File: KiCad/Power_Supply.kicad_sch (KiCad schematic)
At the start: 4 parts, among them J1 USB_B, J2 Jack-DC

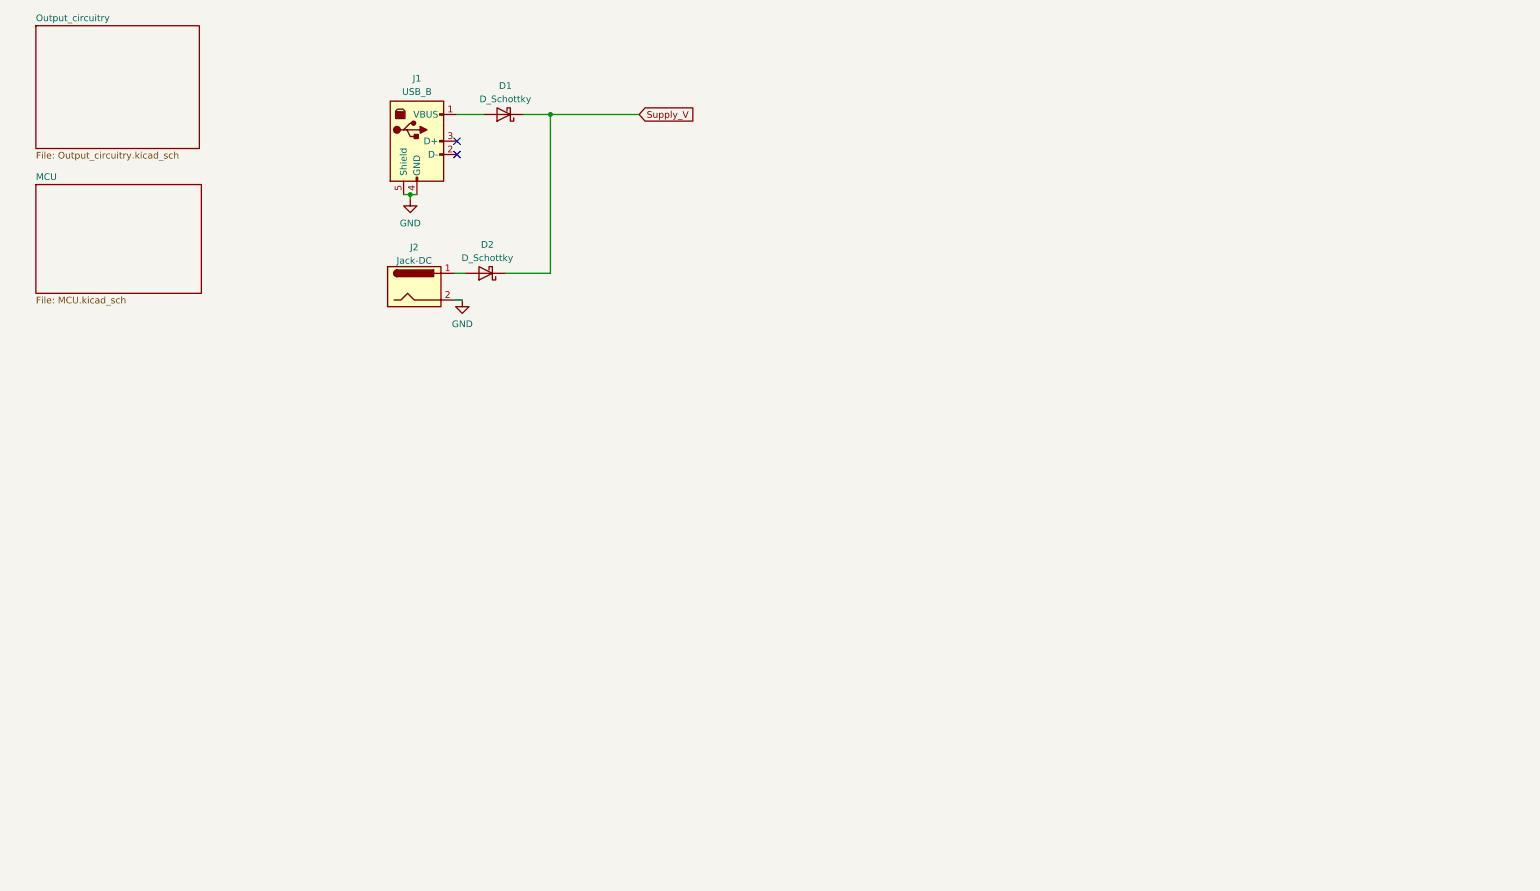
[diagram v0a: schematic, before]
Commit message: Schematic redesign needs two footprints before complete.
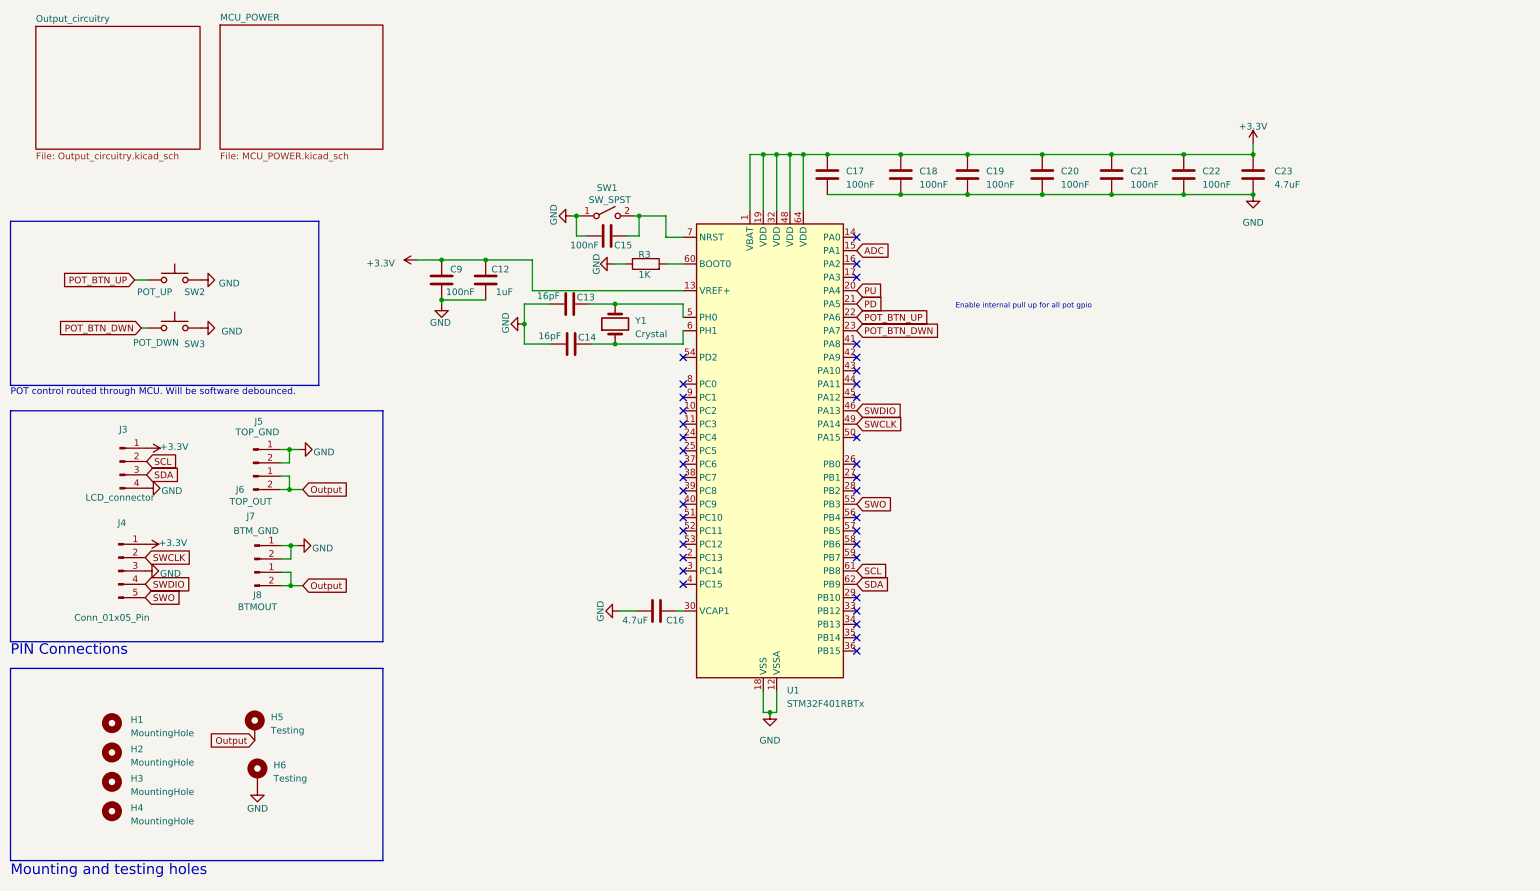
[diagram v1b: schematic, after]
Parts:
- removed D1, D2: D_Schottky, symbol Device:D_Schottky
- removed J1: USB_B, symbol Connector:USB_B
- removed J2: Jack-DC, symbol Connector:Jack-DC
- added C12: 1uF, Capacitor_SMD:C_0603_1608Metric_Pad1.08x0.95mm_HandSolder, symbol Device:C
- added C13, C14: 16pF, Capacitor_SMD:C_0603_1608Metric_Pad1.08x0.95mm_HandSolder, symbol Device:C
- added C15, C17, C18, C19, C20, C21, C22, C9: 100nF, Capacitor_SMD:C_0603_1608Metric_Pad1.08x0.95mm_HandSolder, symbol Device:C
- added C16, C23: 4.7uF, Capacitor_SMD:C_0603_1608Metric_Pad1.08x0.95mm_HandSolder, symbol Device:C
- added H1, H2, H3, H4: MountingHole, MountingHole:MountingHole_3.2mm_M3, symbol Mechanical:MountingHole
- added H5, H6: Testing, MountingHole:MountingHole_2.2mm_M2_DIN965_Pad_TopOnly, symbol Mechanical:MountingHole_Pad
- added J3: LCD_connector, Connector_PinHeader_2.54mm:PinHeader_1x04_P2.54mm_Vertical, symbol Connector:Conn_01x04_Pin
- added J4: Conn_01x05_Pin, Connector_PinHeader_2.54mm:PinHeader_1x05_P2.54mm_Vertical, symbol Connector:Conn_01x05_Pin
- added J5: TOP_GND, Connector_PinHeader_2.54mm:PinHeader_1x02_P2.54mm_Vertical, symbol Connector:Conn_01x02_Pin
- added J6: TOP_OUT, Connector_PinHeader_2.54mm:PinHeader_1x02_P2.54mm_Vertical, symbol Connector:Conn_01x02_Pin
- added J7: BTM_GND, Connector_PinHeader_2.54mm:PinHeader_1x02_P2.54mm_Vertical, symbol Connector:Conn_01x02_Pin
- added J8: BTMOUT, Connector_PinHeader_2.54mm:PinHeader_1x02_P2.54mm_Vertical, symbol Connector:Conn_01x02_Pin
- added R3: 1K, Resistor_SMD:R_0402_1005Metric_Pad0.72x0.64mm_HandSolder, symbol Device:R
- added SW1: SW_SPST, symbol Switch:SW_SPST
- added SW2: POT_UP, Button_Switch_THT:SW_PUSH_6mm_H4.3mm, symbol Switch:SW_Push
- added SW3: POT_DWN, Button_Switch_THT:SW_PUSH_6mm_H4.3mm, symbol Switch:SW_Push
- added U1: STM32F401RBTx, Package_QFP:LQFP-64_10x10mm_P0.5mm, symbol MCU_ST_STM32F4:STM32F401RBTx
- added Y1: Crystal, Crystal:Crystal_SMD_ECS_CSM3X-2Pin_7.6x4.1mm, symbol Device:Crystal
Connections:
- net GND: now also C12.1, C13.1, C14.1, C15.1, C16.1, C17.2, C18.2, C19.2, C20.2, C21.2, C22.2, C23.2, C9.1, H6.1, J3.4 (Pin_4), J4.3 (Pin_3), J5.1 (Pin_1), J5.2 (Pin_2), J7.1 (Pin_1), J7.2 (Pin_2), R3.1, SW1.1 (A), SW2.2, SW3.2, U1.12 (VSSA), U1.18 (VSS), U1.31 (VSS), U1.47 (VSS), U1.63 (VSS)
- new net: C16.2, U1.30 (VCAP1)
- new net: C13.2, U1.5 (PH0), Y1.2
- new net: C14.2, U1.6 (PH1), Y1.1
- new net: R3.2, U1.60 (BOOT0)
- new net: C15.2, SW1.2 (B), U1.7 (NRST)
- new net +3.3V: C12.2, C17.1, C18.1, C19.1, C20.1, C21.1, C22.1, C23.1, C9.2, J3.1 (Pin_1), J4.1 (Pin_1), U1.1 (VBAT), U1.13 (VREF+), U1.19 (VDD), U1.32 (VDD), U1.48 (VDD), U1.64 (VDD)
- new net ADC: U1.15 (PA1)
- new net Output: H5.1, J6.1 (Pin_1), J6.2 (Pin_2), J8.1 (Pin_1), J8.2 (Pin_2)
- new net PD: U1.21 (PA5)
- new net POT_BTN_DWN: SW3.1, U1.23 (PA7)
- new net POT_BTN_UP: SW2.1, U1.22 (PA6)
- new net PU: U1.20 (PA4)
- new net SCL: J3.2 (Pin_2), U1.61 (PB8)
- new net SDA: J3.3 (Pin_3), U1.62 (PB9)
- new net SWCLK: J4.2 (Pin_2), U1.49 (PA14)
- new net SWDIO: J4.4 (Pin_4), U1.46 (PA13)
- new net SWO: J4.5 (Pin_5), U1.55 (PB3)
- no-connect marks 2 -> 38
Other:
- removed sheet MCU
- added sheet MCU_POWER (MCU_POWER.kicad_sch)
- note added: "Enable internal pull up for all pot gpio"
- note added: "Mounting and testing holes"
- note added: "PIN Connections"
- note added: "POT control routed through MCU. Will be software debounced."
- company: (none) -> Eric Mullally
- title: (none) -> Power Supply

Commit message: Board layout preleminary complete.
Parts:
- removed J5: TOP_GND, Connector_PinHeader_2.54mm:PinHeader_1x02_P2.54mm_Vertical, symbol Connector:Conn_01x02_Pin
- removed J6: TOP_OUT, Connector_PinHeader_2.54mm:PinHeader_1x02_P2.54mm_Vertical, symbol Connector:Conn_01x02_Pin
- removed J7: BTM_GND, Connector_PinHeader_2.54mm:PinHeader_1x02_P2.54mm_Vertical, symbol Connector:Conn_01x02_Pin
- removed J8: BTMOUT, Connector_PinHeader_2.54mm:PinHeader_1x02_P2.54mm_Vertical, symbol Connector:Conn_01x02_Pin
- removed SW1: SW_SPST, symbol Switch:SW_SPST
- added J10: BTM_OUT, Connector_PinHeader_2.54mm:PinHeader_2x02_P2.54mm_Vertical, symbol Connector_Generic:Conn_02x02_Top_Bottom
- added J5: TOP_OUT, Connector_PinHeader_2.54mm:PinHeader_2x02_P2.54mm_Vertical, symbol Connector_Generic:Conn_02x02_Top_Bottom
- added R5: 100, Resistor_SMD:R_0402_1005Metric_Pad0.72x0.64mm_HandSolder, symbol Device:R
- added R6: 300, Resistor_SMD:R_0402_1005Metric_Pad0.72x0.64mm_HandSolder, symbol Device:R
- added SW1: NRST, Button_Switch_THT:SW_PUSH_6mm_H4.3mm, symbol Switch:SW_Push
- J4: value Conn_01x05_Pin -> SWD
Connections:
- net ADC: now also R5.2, R6.2; no longer U1.15 (PA1)
- net GND: now also J10.3 (Pin_3), J10.4 (Pin_4), J5.3 (Pin_3), J5.4 (Pin_4), R6.1, SW1.1
- net Output: now also J10.1 (Pin_1), J10.2 (Pin_2), J5.1 (Pin_1), J5.2 (Pin_2)
- net VCAP: now reaches C16.2, U1.30 (VCAP1)
- net BOOT: now reaches R3.2, U1.60 (BOOT0)
- net NRST: now reaches C15.2, U1.7 (NRST)
- net NRST: now also SW1.2
- new net: R5.1, U1.15 (PA1)
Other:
- moved on the sheet: C16, R3

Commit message: Boot-0 and button layout updated.
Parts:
- added R7: 1K, Resistor_SMD:R_0402_1005Metric_Pad0.72x0.64mm_HandSolder, symbol Device:R
- R5: value 100 -> 300
- R6: value 300 -> 1K2
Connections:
- net +3.3V: now also R7.1
- net BOOT: now also R7.2
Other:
- note added: "Notes"
- note removed: "Enable internal pull up for all pot gpio"
- moved on the sheet: C15, SW1

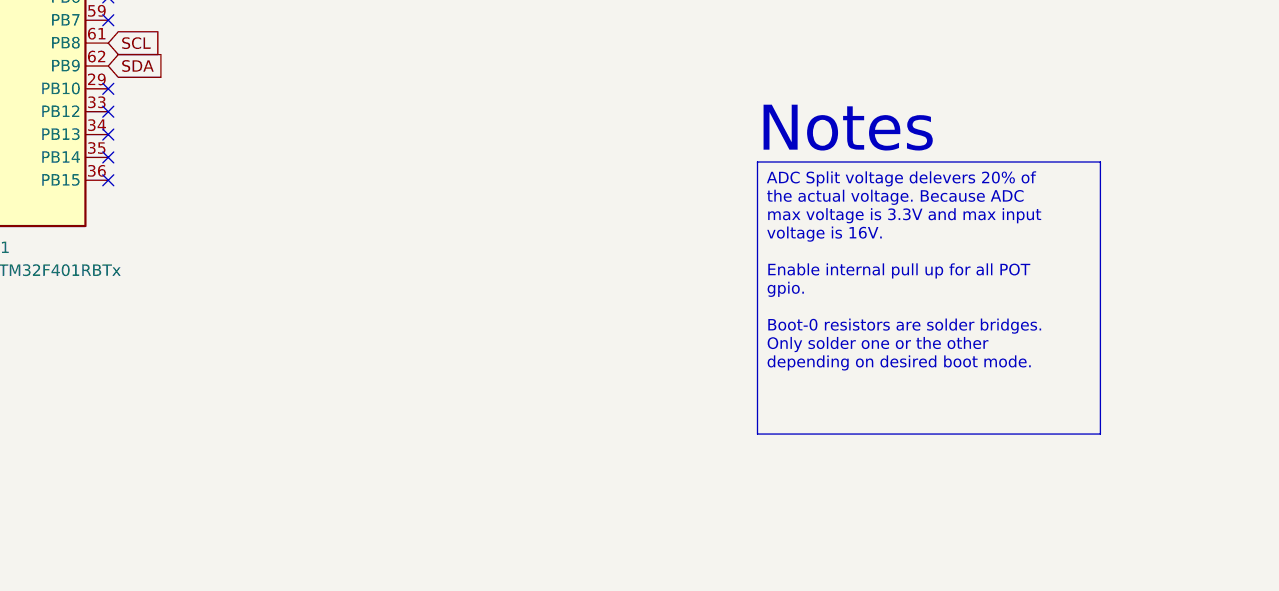
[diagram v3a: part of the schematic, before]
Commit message: Added some notes and extra ground vias.
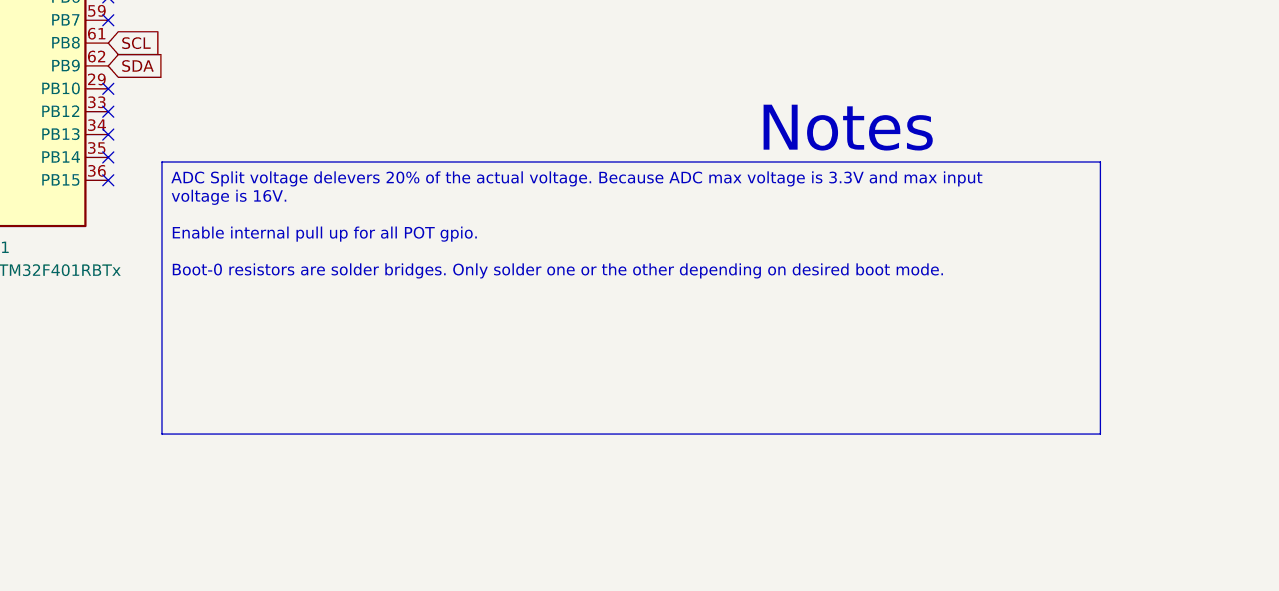
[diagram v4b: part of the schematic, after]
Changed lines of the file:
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@@
   )
   (text_box "ADC Split voltage delevers 20% of the actual voltage. Because ADC max voltage is 3.3V and max input voltage is 16V.\n\nEnable internal pull up for all POT gpio.\n\nBoot-0 resistors are solder bridges. Only solder one or the other depending on desired boot mode."
-    (at 245.872 134.112 0) (size 38.1 30.226)
+    (at 179.705 134.112 0) (size 104.267 30.226)
     (stroke (width 0) (type default))
     (fill (type none))

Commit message: Starting revision 1.1
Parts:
- R5: value 300 -> 2K1
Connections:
- net ADC: now also R5.1; no longer R5.2, R6.2
- net at U1.15 (PA1): now also R5.2, R6.2; no longer R5.1
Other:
- moved on the sheet: R5
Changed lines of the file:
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@@
   (junction (at 194.818 49.276) (diameter 0) (color 0 0 0 0)
   )
+  (junction (at 195.58 59.944) (diameter 0) (color 0 0 0 0)
+  )
   (junction (at 163.576 41.656) (diameter 0) (color 0 0 0 0)
   )
   (junction (at 94.742 69.342) (diameter 0) (color 0 0 0 0)
-  )
-  (junction (at 195.58 59.944) (diameter 0) (color 0 0 0 0)
   )
   (junction (at 168.148 41.656) (diameter 0) (color 0 0 0 0)
@@
     (stroke (width 0) (type default))
   )
-  (wire (pts (xy 195.58 59.944) (xy 192.913 59.944))
+  (wire (pts (xy 173.736 59.944) (xy 195.58 59.944))
     (stroke (width 0) (type default))
   )
@@
     (stroke (width 0) (type default))
   )
-  (wire (pts (xy 185.293 59.944) (xy 173.736 59.944))
-    (stroke (width 0) (type default))
-  )
   (wire (pts (xy 130.048 56.642) (xy 131.572 56.642))
     (stroke (width 0) (type default))
@@
     (stroke (width 0) (type default))
   )
+  (wire (pts (xy 206.248 59.944) (xy 209.804 59.944))
+    (stroke (width 0) (type default))
+  )
   (wire (pts (xy 57.785 100.711) (xy 59.436 100.711))
     (stroke (width 0) (type default))
@@
     (stroke (width 0) (type default))
   )
+  (wire (pts (xy 195.58 59.944) (xy 198.628 59.944))
+    (stroke (width 0) (type default))
+  )
   (wire (pts (xy 209.042 49.276) (xy 222.25 49.276))
     (stroke (width 0) (type default))
@@
     (stroke (width 0) (type default))
   )
-  (wire (pts (xy 198.755 59.944) (xy 195.58 59.944))
-    (stroke (width 0) (type default))
-  )
   (wire (pts (xy 121.666 45.466) (xy 119.634 45.466))
     (stroke (width 0) (type default))
@@
     (fill (type none))
   )
-  (text_box "ADC Split voltage delevers 20% of the actual voltage. Because ADC max voltage is 3.3V and max input voltage is 16V.\n\nEnable internal pull up for all POT gpio.\n\nBoot-0 resistors are solder bridges. Only solder one or the other depending on desired boot mode."
+  (text_box "ADC max input is 3.3V max output of TPS63070RNMR is 9V \n \nEnable internal pull up for all POT gpio.\n\nBoot-0 resistors are solder bridges. Only solder one or the other depending on desired boot mode."
     (at 179.705 134.112 0) (size 104.267 30.226)
     (stroke (width 0) (type default))
@@
     )
   )
-  (global_label "ADC" (shape input) (at 198.755 59.944 0) (fields_autoplaced)
-    (effects (font (size 1.27 1.27)) (justify left))
-    (property "Intersheetrefs" "${INTERSHEET_REFS}" (at 205.2894 59.944 0)
+  (global_label "ADC" (shape input) (at 209.804 59.944 0) (fields_autoplaced)
+    (effects (font (size 1.27 1.27)) (justify left))
+    (property "Intersheetrefs" "${INTERSHEET_REFS}" (at 216.3384 59.944 0)
       (effects (font (size 1.27 1.27)) (justify left) hide)
     )
@@
     )
   )
-  (symbol (lib_id "Device:R") (at 189.103 59.944 90) (unit 1)
-    (in_bom yes) (on_board yes) (dnp no)
-    (property "Reference" "R5" (at 188.849 58.166 90)
-      (effects (font (size 1.27 1.27)))
-    )
-    (property "Value" "300" (at 188.849 61.976 90)
-      (effects (font (size 1.27 1.27)))
-    )
-    (property "Footprint" "Resistor_SMD:R_0402_1005Metric_Pad0.72x0.64mm_HandSolder" (at 189.103 61.722 90)
-      (effects (font (size 1.27 1.27)) hide)
-    )
-    (property "Datasheet" "~" (at 189.103 59.944 0)
-      (effects (font (size 1.27 1.27)) hide)
-    )
+  (symbol (lib_id "Device:R") (at 202.438 59.944 270) (unit 1)
+    (in_bom yes) (on_board yes) (dnp no)
+    (property "Reference" "R5" (at 202.692 61.722 90)
+      (effects (font (size 1.27 1.27)))
+    )
+    (property "Value" "2K1" (at 202.692 57.912 90)
+      (effects (font (size 1.27 1.27)))
+    )
+    (property "Footprint" "Resistor_SMD:R_0402_1005Metric_Pad0.72x0.64mm_HandSolder" (at 202.438 58.166 90)
+      (effects (font (size 1.27 1.27)) hide)
+    )
+    (property "Datasheet" "~" (at 202.438 59.944 0)
+      (effects (font (size 1.27 1.27)) hide)
+    )

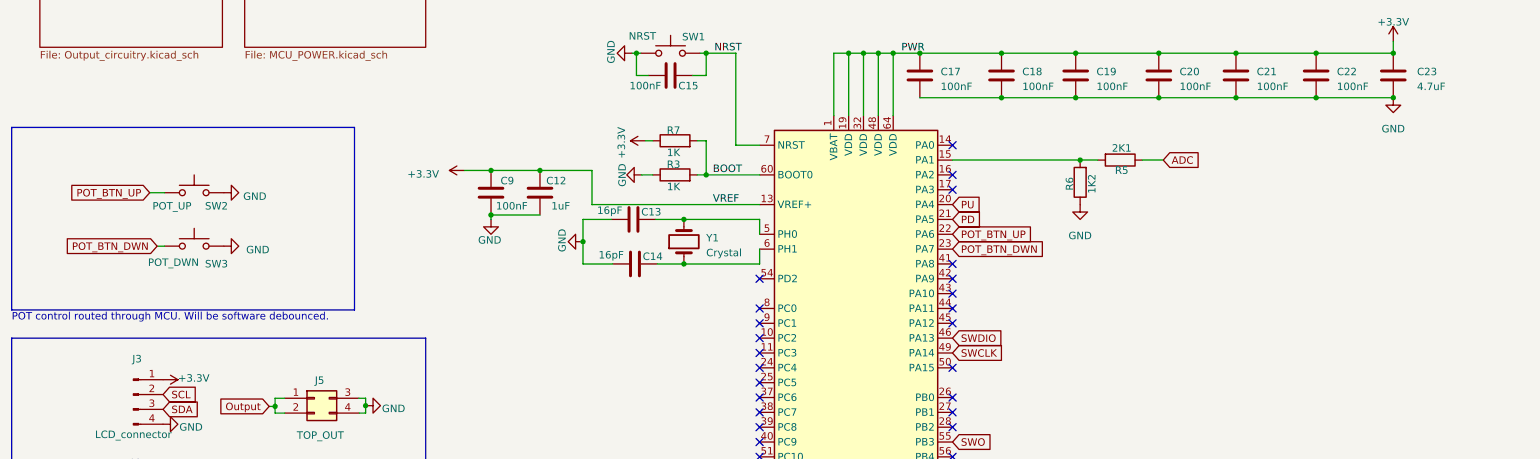
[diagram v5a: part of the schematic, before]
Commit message: Replaced pot.
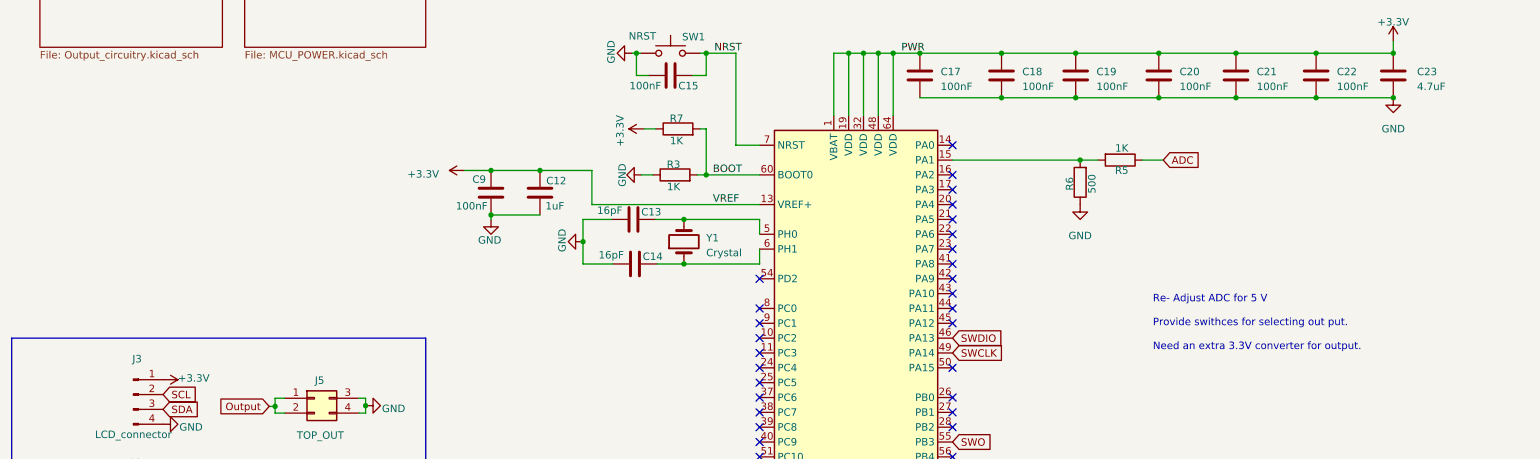
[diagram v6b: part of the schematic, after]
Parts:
- removed SW2: POT_UP, Button_Switch_THT:SW_PUSH_6mm_H4.3mm, symbol Switch:SW_Push
- removed SW3: POT_DWN, Button_Switch_THT:SW_PUSH_6mm_H4.3mm, symbol Switch:SW_Push
- R5: value 2K1 -> 1K
- R6: value 1K2 -> 500
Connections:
- net PD: no longer names the net of U1.21 (PA5)
- net POT_BTN_DWN: no longer names the net of U1.23 (PA7)
- net POT_BTN_UP: no longer names the net of U1.22 (PA6)
- net PU: no longer names the net of U1.20 (PA4)
- no-connect marks 38 -> 42
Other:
- note added: "Re- Adjust ADC for 5 V Provide swithces for selecting out put. Need an extra 3.3V converter for output."
- note removed: "POT control routed through MCU. Will be software debounced."
- moved on the sheet: R7
